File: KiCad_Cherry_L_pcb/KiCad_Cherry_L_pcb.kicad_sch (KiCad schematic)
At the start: 63 parts, among them J1 AudioJack3_SwitchTR, SW1 Esc, SW10 E, SW11 R, SW12 T, SW13 Ctrl, SW14 A, SW15 S, SW16 D, SW17 F, SW18 G, SW19 Shift, SW2 1, SW20 Z, SW21 X, SW22 C, SW23 V, SW24 6, SW25 Fn, SW26 Alt, SW27 Win, SW28 NoConv, SW29 Space, SW3 2, SW4 3, SW5 4, SW6 5, SW7 Tab, SW8 Q, SW9 W, U1 Sparkfun_Pro_Micro

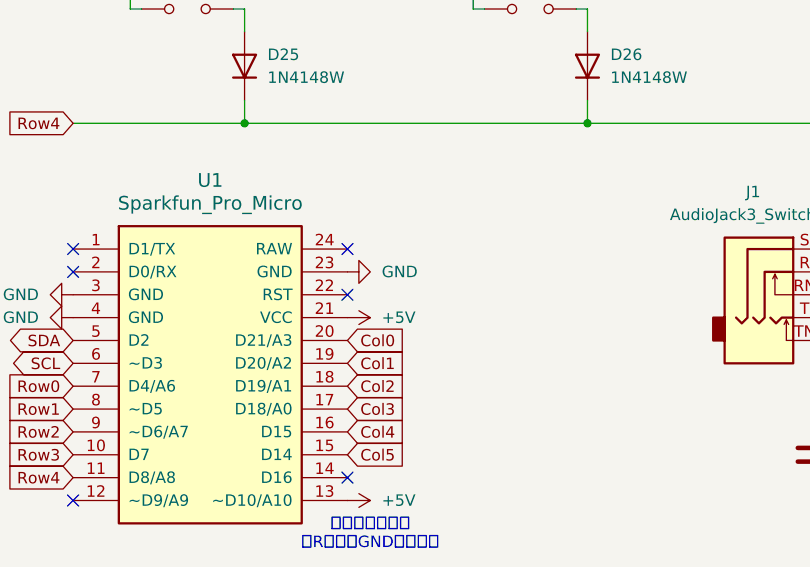
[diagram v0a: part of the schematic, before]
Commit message: feat: Resetピンを追加
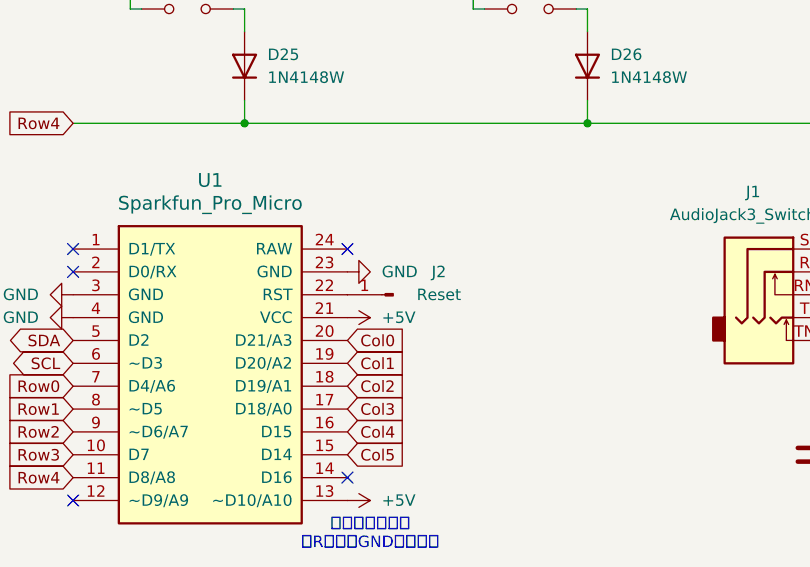
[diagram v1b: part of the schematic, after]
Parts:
- added J2: Reset, Connector_PinHeader_1.00mm:PinHeader_1x01_P1.00mm_Vertical, symbol Connector:Conn_01x01_Pin
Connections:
- net at U1.22 (RST): now also J2.1 (Pin_1)
- no-connect marks 8 -> 7
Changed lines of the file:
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@@
 	)
 	(no_connect
-		(at 74.93 165.1)
-	)
-	(no_connect
 		(at 44.45 162.56)
 	)
@@
 	)
 	(symbol
+		(lib_id "power:GND")
+		(at 74.93 162.56 90)
+		(mirror x)
+		(unit 1)
+		(exclude_from_sim no)
+		(in_bom yes)
+		(on_board yes)
+		(dnp no)
+		(property "Reference" "#PWR02"
+			(at 81.28 162.56 0)
+			(effects
+				(font
+					(size 1.27 1.27)
+				)
+				(hide yes)
+			)
+		)
+		(property "Value" "GND"
+			(at 78.74 162.5599 90)
+			(effects
+				(font
+					(size 1.27 1.27)
+				)
+				(justify right)
+			)
+		)
+		(property "Footprint" ""
+			(at 74.93 162.56 0)
+			(effects
+				(font
+					(size 1.27 1.27)
+				)
+				(hide yes)
+			)
+		)
+		(property "Datasheet" ""
+			(at 74.93 162.56 0)
+			(effects
+				(font
+					(size 1.27 1.27)
+				)
+				(hide yes)
+			)
+		)
+		(property "Description" "Power symbol creates a global label with name \"GND\" , ground"
+			(at 74.93 162.56 0)
+			(effects
+				(font
+					(size 1.27 1.27)
+				)
+				(hide yes)
+			)
+		)
+		(pin "1"
+		)
+		(instances
+			(project "KiCad_Cherry_L_pcb"
+				(path "/63624602-85c8-4a35-8071-08b2ca90618c"
+					(reference "#PWR02")
+					(unit 1)
+				)
+			)
+		)
+	)
+	(symbol
 		(lib_id "Switch:SW_Push")
 		(at 95.25 82.55 0)
@@
 	(symbol
 		(lib_id "power:GND")
-		(at 74.93 162.56 90)
-		(unit 1)
-		(exclude_from_sim no)
-		(in_bom yes)
-		(on_board yes)
-		(dnp no)
-		(fields_autoplaced yes)
-		(property "Reference" "#PWR02"
-			(at 81.28 162.56 0)
-			(effects
-				(font
-					(size 1.27 1.27)
-				)
-				(hide yes)
-			)
-		)
-		(property "Value" "GND"
-			(at 78.74 162.5599 90)
-			(effects
-				(font
-					(size 1.27 1.27)
-				)
-				(justify right)
-			)
-		)
-		(property "Footprint" ""
-			(at 74.93 162.56 0)
-			(effects
-				(font
-					(size 1.27 1.27)
-				)
-				(hide yes)
-			)
-		)
-		(property "Datasheet" ""
-			(at 74.93 162.56 0)
-			(effects
-				(font
-					(size 1.27 1.27)
-				)
-				(hide yes)
-			)
-		)
-		(property "Description" "Power symbol creates a global label with name \"GND\" , ground"
-			(at 74.93 162.56 0)
-			(effects
-				(font
-					(size 1.27 1.27)
-				)
-				(hide yes)
-			)
-		)
-		(pin "1"
-		)
-		(instances
-			(project "KiCad_Cherry_L_pcb"
-				(path "/63624602-85c8-4a35-8071-08b2ca90618c"
-					(reference "#PWR02")
-					(unit 1)
-				)
-			)
-		)
-	)
-	(symbol
-		(lib_id "power:GND")
 		(at 146.05 187.96 0)
 		(unit 1)
@@
 					(unit 1)
 				)
+			)
+		)
+	)
+	(symbol
+		(lib_id "Connector:Conn_01x01_Pin")
+		(at 80.01 165.1 0)
+		(mirror y)
+		(unit 1)
+		(exclude_from_sim no)
+		(in_bom yes)
+		(on_board yes)
+		(dnp no)
+		(property "Reference" "J2"
+			(at 85.09 162.56 0)
+			(effects
+				(font
+					(size 1.27 1.27)
+				)
+			)
+		)
+		(property "Value" "Reset"
+			(at 85.09 165.1 0)
+			(effects
+				(font
+					(size 1.27 1.27)
+				)
+			)
+		)
+		(property "Footprint" "Connector_PinHeader_1.00mm:PinHeader_1x01_P1.00mm_Vertical"
+			(at 80.01 165.1 0)
+			(effects
+				(font
+					(size 1.27 1.27)
+				)
+				(hide yes)
+			)
+		)
+		(property "Datasheet" "~"
+			(at 80.01 165.1 0)
+			(effects
+				(font
+					(size 1.27 1.27)
+				)
+				(hide yes)
+			)
+		)
+		(property "Description" "Generic connector, single row, 01x01, script generated"
+			(at 80.01 165.1 0)
+			(effects
+				(font
+					(size 1.27 1.27)
+				)
+				(hide yes)
+			)
+		)
+		(pin "1"
+		)
+		(instances
+			(project "KiCad_Cherry_L_pcb"
+				(path "/63624602-85c8-4a35-8071-08b2ca90618c"
+					(reference "J2")
+					(unit 1)
+				)
